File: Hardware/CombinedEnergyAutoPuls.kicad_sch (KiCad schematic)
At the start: 0 parts

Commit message: STAGE: Schematics finished
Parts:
- added A1: Arduino_Ethernet, Local_MCU_Module_Library:Arduino_Ethernet_WithMountingHoles, symbol Local_MCU_Module_Library:Arduino_Ethernet
- added C1: C10uf, Capacitor_SMD:C_0603_1608Metric, symbol Local_Device_Library:C10uf
- added C2: C330nf, Capacitor_SMD:C_0805_2012Metric, symbol Local_Device_Library:C330nf
- added C3: C100nf, Capacitor_SMD:C_0402_1005Metric, symbol Local_Device_Library:C100nf
- added D1, D2, D3, D4, D5, D6, D7, D8: 1N4148WS, Diode_SMD:D_SOD-323F, symbol Local_Diode_Library:1N4148WS
- added D10: D_Z2V7, Diode_THT:D_DO-34_SOD68_P7.62mm_Horizontal, symbol Local_Diode_Library:D_Z2V4
- added D11: 1N4004, Diode_THT:D_DO-41_SOD81_P12.70mm_Horizontal, symbol Local_Diode_Library:1N4004
- added D9: LED_G3, LED_THT:LED_D3.0mm, symbol Local_Diode_Library:LED_G3
- added J1, J2, J6: Screw_Terminal_01x04, Local_Connectors:TerminalBlock_PT-1,5-4-5.0-H_1x04_P5.00mm_Horizontal-(F.Mount), symbol Local_Connectors_Library:Screw_Terminal_01x04
- added J3: Arduino_USB-Serial_Card, Local_Connectors:Arduino_USB-Serial_Card, symbol Local_Connectors_Library:Arduino_USB-Serial_Card_Connector
- added J4: Arduino_USB-Serial_Card_Connector, Local_Connectors:Arduino_USB-Serial_Card_EdgeConn, symbol Local_Connectors_Library:Arduino_USB-Serial_Card_Connector
- added J5: AudioJack3_Switch, Local_Connectors:AUDIO_JACK_ASJ-195-L-HT-(F.Mount), symbol Local_Connectors_Library:AudioJack3_Switch
- added JP1: Jumper_3_Bridged12, Connector_PinHeader_2.54mm:PinHeader_1x03_P2.54mm_Vertical, symbol Local_Connectors_Library:Jumper_3_Bridged12
- added Q1: S8550_PNP, Package_TO_SOT_SMD:SOT-23, symbol Local_Transistor_BJT_Library:S8550_PNP
- added Q2, Q3: S8050_NPN, Package_TO_SOT_SMD:SOT-23, symbol Local_Transistor_BJT_Library:S8050_NPN
- added R1, R8, R9: R10K, Resistor_SMD:R_0402_1005Metric, symbol Local_Device_Library:R10K
- added R2: R680K, Resistor_SMD:R_0603_1608Metric, symbol Local_Device_Library:R680K
- added R3: R39K, Resistor_SMD:R_0402_1005Metric, symbol Local_Device_Library:R39K
- added R4, R5: R180K, Resistor_SMD:R_0603_1608Metric, symbol Local_Device_Library:R180K
- added R6: R220, Resistor_SMD:R_0805_2012Metric, symbol Local_Device_Library:R220
- added R7: R56, Resistor_SMD:R_1206_3216Metric, symbol Local_Device_Library:R56
- added U1: L78S05CV, Package_TO_SOT_THT:TO-220-3_Vertical, symbol Local_Miscellaneous_Library:L78S05CV
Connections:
- new net: Q1.1 (B), R2.2
- new net: Q1.3 (C), R4.1
- new net: D11.2 (A), J6.1 (Pin_1)
- new net: J5.1 (S), R8.2, R9.1
- new net: Q2.1 (B), R3.1, R4.2
- new net: A1.7 (A0), D3.1 (K), J2.2 (Pin_2)
- new net: D1.2 (A), D2.2 (A), D3.2 (A), D4.2 (A), D5.2 (A), D6.2 (A), D7.2 (A), D8.2 (A), R1.2, R2.1
- new net: A1.8 (A1), D2.1 (K), J2.3 (Pin_3)
- new net: A1.30 (N/C), J4.2 (N/C)
- new net: A1.32 (TXD), J4.4 (TXD)
- new net: A1.33 (RXD), J4.5 (RXD)
- new net: A1.34 (~{RTS}), J4.6 (DRT)
- new net: A1.19 (D6), D6.1 (K), J1.3 (Pin_3)
- new net: C1.1, J5.2 (T), JP1.3 (B), R7.1
- new net: A1.16 (D3/INT1), D8.1 (K), J1.1 (Pin_1)
- new net: A1.18 (D5), D7.1 (K), J1.2 (Pin_2)
- new net: A1.20 (D7), D5.1 (K), J1.4 (Pin_4)
- new net: A1.6 (VIN), C2.1, R6.1, U1.3 (VO)
- new net: D9.2 (A), R6.2
- new net: A1.21 (D8), D4.1 (K), J2.1 (Pin_1)
- new net: D1.1 (K), J2.4 (Pin_4), JP1.1 (A)
- new net: D9.1 (K), Q3.3 (C)
- new net: A1.15 (D2/INT0), Q2.3 (C)
- new net: A1.10 (A3), R5.1
- new net: Q3.1 (B), R5.2
- new net: A1.9 (A2), JP1.2 (C)
- new net +24V: C3.1, D11.1 (K), U1.1 (VI)
- new net +5V: A1.3 (+5V), Q1.2 (E), R1.1, R8.1
- new net GND: A1.27 (GND), A1.29 (GND_BLK), A1.4 (GND), A1.5 (GND), C1.2, D10.2 (A), J4.1 (GND), J5.5 (R), J6.2 (Pin_2), Q2.2 (E), Q3.2 (E), R3.2, R7.2, R9.2
- new net GND1: C2.2, C3.2, D10.1 (K), U1.2 (GND)
- new net VCC: A1.31 (VCC), J4.3 (VCC)
- no-connect marks 0 -> 25

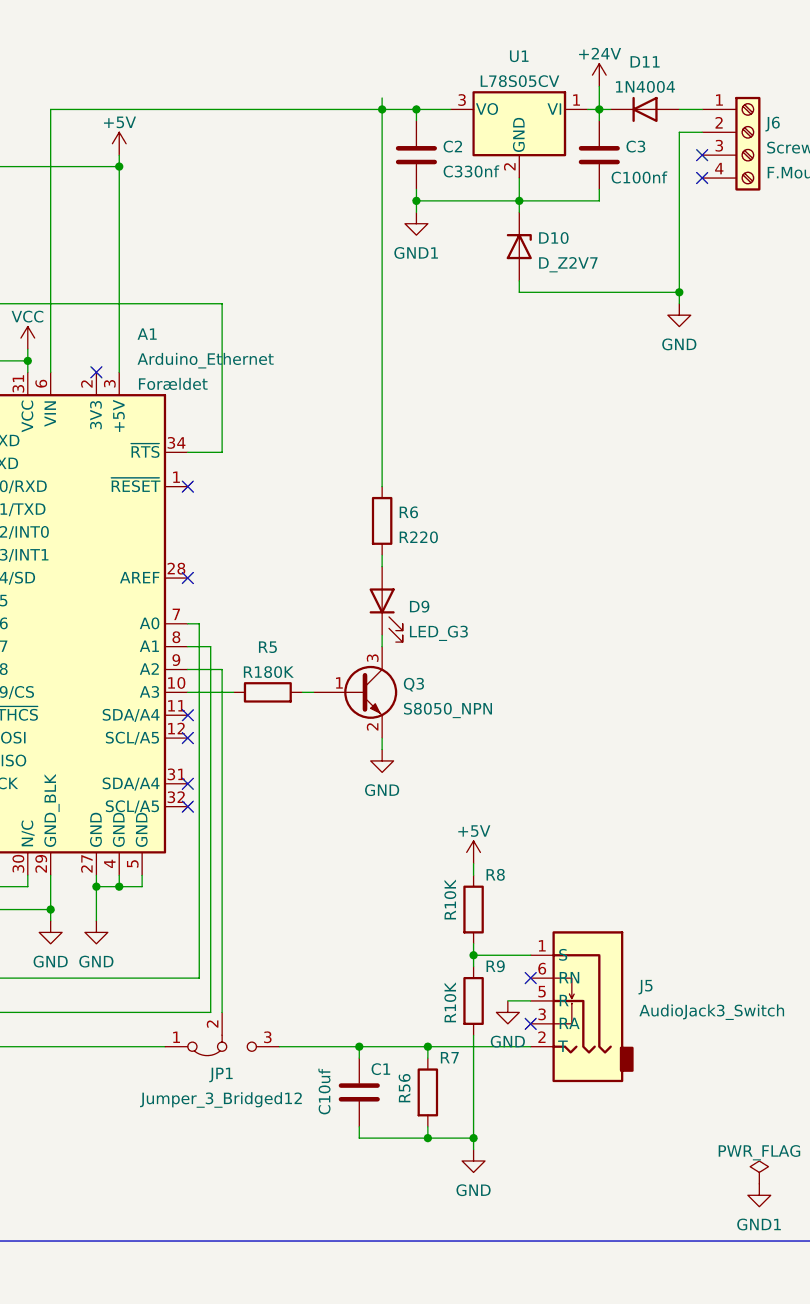
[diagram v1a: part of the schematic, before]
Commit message: FIX: Fixes made to local libraies
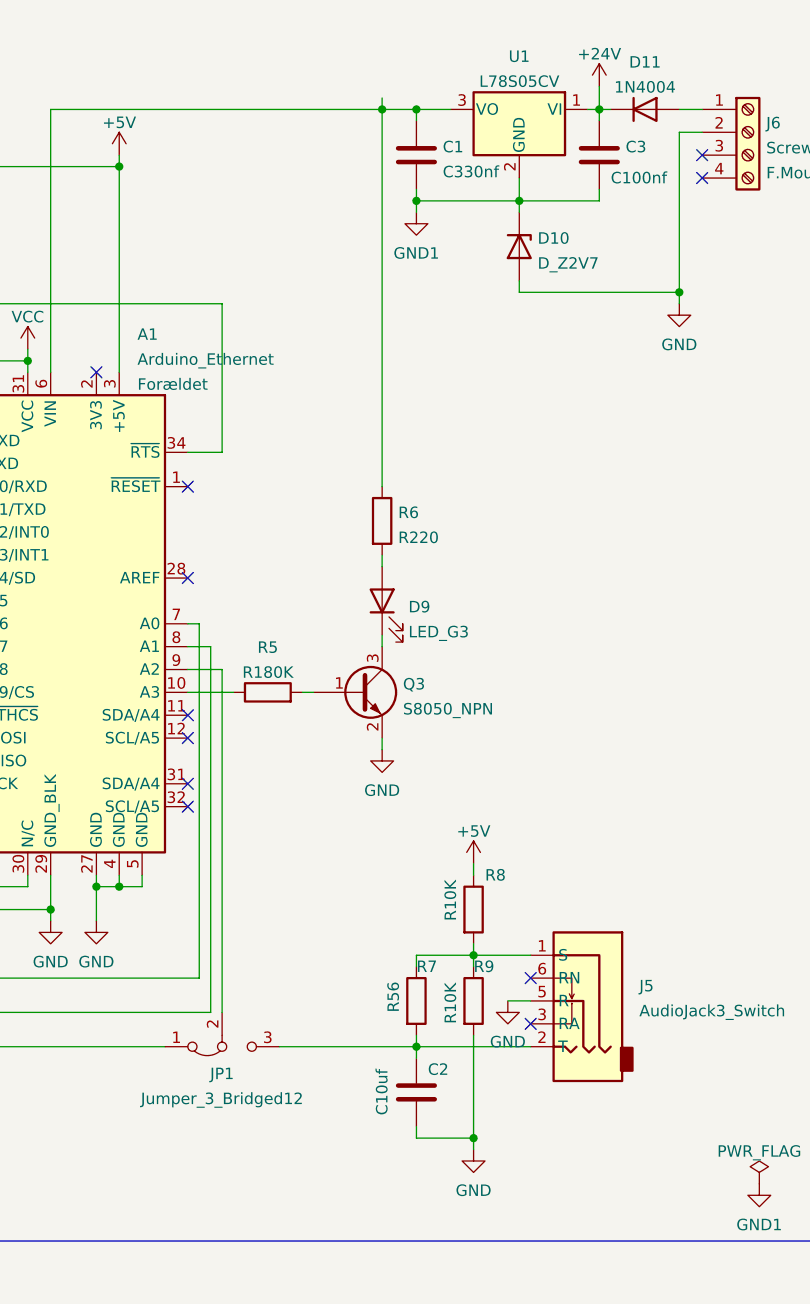
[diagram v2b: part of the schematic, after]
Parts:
- renumbered C2 to C1, C1 to C2
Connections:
- net GND: no longer R7.2
- net at J5.1 (S), R8.2, R9.1: now also R7.1
- net at C2.1, J5.2 (T), JP1.3 (B): now also R7.2; no longer R7.1
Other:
- moved on the sheet: C2, R7

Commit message: Schematics and components placed on BCB for autoStart added to the project.
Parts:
- added C101: C10nf, Capacitor_SMD:C_0402_1005Metric, symbol Local_Device_Library:C10nf
- added C102, C103, C104: C100nf, Capacitor_SMD:C_0402_1005Metric, symbol Local_Device_Library:C100nf
- added C105: C330nf, Capacitor_SMD:C_0805_2012Metric, symbol Local_Device_Library:C330nf
- added D101: 1N4148WS, Diode_SMD:D_SOD-323F, symbol Local_Diode_Library:1N4148WS
- added J101: AudioJack3_Switch, Local_Connectors:AUDIO_JACK_ASJ-195-L-HT-(B.Mount), symbol Local_Connectors_Library:AudioJack3_Switch
- added J102: Screw_Terminal_01x03, Local_Connectors:Phoenix_TERM_BLOCK_3POS_45DEG_5MM_PCB-(B.Mount), symbol Local_Connectors_Library:Screw_Terminal_01x03
- added J103: Conn_3P, Local_Connectors:PinHeader_1x03_P_5mm_Vertical-(F.Mount), symbol Local_Connectors_Library:Conn_3P
- added J3: Pin_Header_1x6, Local_Connectors:PinHeader_1x06_P_0,1in_Vertical, symbol Local_Connectors_Library:Pin_Header_1x6
- added Q101: S8050, Package_TO_SOT_SMD:SOT-23, symbol Local_Transistor_BJT_Library:S8050_NPN
- added R101, R102, R103: R10K, Resistor_SMD:R_0402_1005Metric, symbol Local_Device_Library:R10K
- added R104: R330K, Resistor_SMD:R_0402_1005Metric, symbol Local_Device_Library:R330K
- added R105: R100K, Resistor_SMD:R_0402_1005Metric, symbol Local_Device_Library:R100K
- added R106: R680K, Resistor_SMD:R_0603_1608Metric, symbol Local_Device_Library:R680K
- added R107: R150K, Resistor_SMD:R_0402_1005Metric, symbol Local_Device_Library:R150K
- added R108: R33K, Resistor_SMD:R_0402_1005Metric, symbol Local_Device_Library:R33K
- added R109: R180K, Resistor_SMD:R_0603_1608Metric, symbol Local_Device_Library:R180K
- added U101: LM358DR2G, Package_SO:SOIC-8_3.9x4.9mm_P1.27mm, symbol Local_Miscellaneous_Library:LM358DR2G
- added U102: 78L05, Package_TO_SOT_SMD:SOT-89-3, symbol Local_Miscellaneous_Library:78L05
- renumbered J3 to J4, J4 to J5, J5 to J6, J6 to J7
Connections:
- net GND3: now reaches J4.1 (GND)
- net GND3: now also J3.1 (Pin_1)
- net at J4.2 (N/C): now also J3.2 (Pin_2)
- net VCC1: now reaches J4.3 (VCC)
- net VCC1: now also J3.3 (Pin_3)
- net at J4.4 (TXD): now also J3.4 (Pin_4)
- net at J4.5 (RXD): now also J3.5 (Pin_5)
- net at J4.6 (DRT): now also J3.6 (Pin_6)
- new net: C103.2, D101.1 (K), R106.1, U101.5 (+)
- new net: R107.2, R108.1, U101.6 (-)
- new net: R109.1, U101.7
- new net: J102.2 (Pin_2), J103.2 (Pin_2), Q101.3 (C)
- new net: C102.2, D101.2 (A), R105.1
- new net: J101.1 (S), R101.1
- new net: C101.1, R101.2, R104.1, U101.3 (+)
- new net: C101.2, C102.1, R104.2, U101.1
- new net: J101.2 (T), R102.2, R103.1, U101.2 (-)
- new net: Q101.1 (B), R109.2
- new net GND2: C103.1, C104.1, C105.2, J101.5 (R), J102.1 (Pin_1), J103.1 (Pin_1), Q101.2 (E), R103.2, R105.2, R106.2, R108.2, U101.4 (V-), U102.2 (GND)
- new net VS: C104.2, R102.1, R107.1, U101.8 (V+), U102.1 (OUT)
- new net VSS: C105.1, J102.3 (Pin_3), J103.3 (Pin_3), U102.3 (IN)
- no-connect marks 25 -> 21
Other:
- moved on the sheet: J4

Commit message: UPD: - Schematics and components placed on BCB for ProgrameablePulseGenerator added to the project
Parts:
- removed J4: Arduino_USB-Serial_Card, Local_Connectors:Arduino_USB-Serial_Card, symbol Local_Connectors_Library:Arduino_USB-Serial_Card_Connector
- removed J5: Arduino_USB-Serial_Card_Connector, Local_Connectors:Arduino_USB-Serial_Card_EdgeConn, symbol Local_Connectors_Library:Arduino_USB-Serial_Card_Connector
- added A201: Arduino_Nano_v3, Module:Arduino_Nano, symbol Local_MCU_Module_Library:Arduino_Nano_v3
- added AE201: Antenna, Local_Misckllaneous_Library:Undefined_Antenna(B.Mount), symbol Local_Miscellaneous_Library:Antenna
- added C201: C100nf, Capacitor_SMD:C_0402_1005Metric, symbol Local_Device_Library:C100nf
- added C202: C330nf, Capacitor_SMD:C_0805_2012Metric, symbol Local_Device_Library:C330nf
- added D201, D203, D205, D207, D209, D211, D213, D215, D217, D219: 1N4148WS, Diode_SMD:D_SOD-323F, symbol Local_Diode_Library:1N4148WS
- added D202, D204, D206, D208, D210, D212, D214, D216, D218, D220: LED, LED_SMD:LED_0805_2012Metric, symbol Local_Diode_Library:LED_0805_R
- added J201, J202: Conn_20P_Female, Connector_PinHeader_2.54mm:PinHeader_1x20_P2.54mm_Vertical, symbol Local_Connectors_Library:Conn_20P_Female
- added J203, J204: Conn_4P_Female, Connector_PinHeader_2.54mm:PinHeader_1x04_P2.54mm_Vertical, symbol Local_Connectors_Library:Conn_4P_Female
- added J205: Barrel_Jack_Switch, Local_Connectors:BarrelJack_Horizontal(F.Mount), symbol Local_Connectors_Library:Barrel_Jack_Switch
- added J4: Arduino_USB-Serial_Card_Connector, Local_Connectors:Arduino_USB-Serial_Card, symbol Local_Connectors_Library:Arduino_USB-Serial_Card-Edge_Connector
- added J5: Arduino_USB-Serial_Edge_Connector, Local_Connectors:Arduino_USB-Serial_Card_EdgeConn, symbol Local_Connectors_Library:Arduino_USB-Serial_Card-Edge_Connector
- added JP201, JP202, JP203, JP204, JP205, JP206, JP207, JP208, JP209, JP210: SolderJumper, Local_Connectors:SolderJumper-2_P1.3mm_Bridged_RoundedPad1.0x1.5mm(B.Mount), symbol Local_Connectors_Library:SolderJumper_2_Bridged
- added JP211: Jumper_3_Bridged12, Connector_PinHeader_2.54mm:PinHeader_1x03_P2.54mm_Vertical, symbol Local_Connectors_Library:Jumper_3_Bridged12
- added R201, R203, R205, R207, R209, R211, R213, R215, R217, R219, R221: R390, Resistor_SMD:R_0603_1608Metric, symbol Local_Device_Library:R390
- added R202, R204, R206, R208, R210, R212, R214, R216, R218, R220: R180, Resistor_SMD:R_0805_2012Metric, symbol Local_Device_Library:R180
- added SW201: THT_SW_4_Tactile, Local_Misckllaneous_Library:THT_SW_Tactile(F.Mount), symbol Local_Miscellaneous_Library:THT_SW_4_Tactile
- added U201, U202, U203, U204, U205, U206, U207, U208, U209, U210, U211: PC817, Local_Misckllaneous_Library:DIP-4_W7.62mm_Slim(F.Mount), symbol Local_Miscellaneous_Library:PC817
- added U212: L78S05CV, Package_TO_SOT_THT:TO-220-3_Vertical, symbol Local_Miscellaneous_Library:L78S05CV
- D10: value D_Z2V7 -> D_Z2V4; footprint Diode_THT:D_DO-34_SOD68_P7.62mm_Horizontal -> Diode_THT:D_DO-35_SOD27_P7.62mm_Horizontal; JLCPCB Part # C294824 -> C2504; MFR. Part # GDZJ12C_AY_10001 -> BZX55C2V4; Manufacturer PANJIT International -> ST(Semtech)
- J101, J102, J103, J3: now left out of the parts list
- Q101: value S8050 -> S8050_NPN
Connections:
- net GND: now also J5.1 (GND)
- net GND3: now also J4.1 (GND)
- net VCC: now also J5.3 (VCC)
- net VCC1: now also J4.3 (VCC)
- net at A1.30 (N/C): now also J5.2 (N/C)
- net at A1.33 (RXD): now also J5.5 (RXD)
- net at A1.34 (~{RTS}): now also J5.6 (DRT)
- net at J3.2 (Pin_2): now also J4.2 (N/C)
- net at J3.4 (Pin_4): now also J4.4 (TXD)
- net at J3.5 (Pin_5): now also J4.5 (RXD)
- net at J3.6 (Pin_6): now also J4.6 (DRT)
- new net: R203.2, U202.1
- new net: JP211.2 (C), R202.1, R204.1, R206.1, R208.1, R210.1, R212.1, R214.1, R216.1, R218.1, R220.1
- new net: C201.1, JP211.3 (B), U212.3 (VO)
- new net: D204.2 (A), R204.2
- new net: A201.14 (D11), D220.1 (K), J201.19 (Pin_19), J201.20 (Pin_20), U210.2
- new net: D220.2 (A), R220.2
- new net: R201.2, U201.1
- new net: A201.5 (D2), D202.1 (K), J201.1 (Pin_1), J201.2 (Pin_2), U201.2
- new net: J202.1 (Pin_1), J202.2 (Pin_2), JP201.2 (B), U201.4
- new net: D209.1 (K), JP205.1 (A)
- new net: D201.2 (A), D203.2 (A), D205.2 (A), D207.2 (A), D209.2 (A), D211.2 (A), D213.2 (A), D215.2 (A), D217.2 (A), D219.2 (A), U211.2
- new net: R217.2, U209.1
- new net: A201.6 (D3), D204.1 (K), J201.3 (Pin_3), J201.4 (Pin_4), U202.2
- new net: A201.8 (D5), D208.1 (K), J201.7 (Pin_7), J201.8 (Pin_8), U204.2
- new net: D208.2 (A), R208.2
- new net: R221.2, U211.1
- new net: A201.13 (D10), D218.1 (K), J201.17 (Pin_17), J201.18 (Pin_18), U209.2
- new net: J202.17 (Pin_17), J202.18 (Pin_18), JP209.2 (B), U209.4
- new net: D202.2 (A), R202.2
- new net: D218.2 (A), R218.2
- new net: D214.2 (A), R214.2
- new net: A201.24 (A5), SW201.1, SW201.2
- new net: D215.1 (K), JP208.1 (A)
- new net: R219.2, U210.1
- new net: R213.2, U207.1
- new net: D207.1 (K), JP204.1 (A)
- new net: J202.7 (Pin_7), J202.8 (Pin_8), JP204.2 (B), U204.4
- new net: D205.1 (K), JP203.1 (A)
- new net: D213.1 (K), JP207.1 (A)
- new net: J202.13 (Pin_13), J202.14 (Pin_14), JP207.2 (B), U207.4
- new net: D211.1 (K), JP206.1 (A)
- new net: J202.11 (Pin_11), J202.12 (Pin_12), JP206.2 (B), U206.4
- new net: D217.1 (K), JP209.1 (A)
- new net: R209.2, U205.1
- new net: A201.9 (D6), D210.1 (K), J201.10 (Pin_10), J201.9 (Pin_9), U205.2
- new net: J202.10 (Pin_10), J202.9 (Pin_9), JP205.2 (B), U205.4
- new net: A201.7 (D4), D206.1 (K), J201.5 (Pin_5), J201.6 (Pin_6), U203.2
- new net: D206.2 (A), R206.2
- new net: J202.19 (Pin_19), J202.20 (Pin_20), JP210.2 (B), U210.4
- new net: R205.2, U203.1
- new net: J202.5 (Pin_5), J202.6 (Pin_6), JP203.2 (B), U203.4
- new net: R215.2, U208.1
- new net: J203.3 (Pin_3), J204.3 (Pin_3)
- new net: J203.4 (Pin_4), J204.4 (Pin_4), U211.4
- new net: D203.1 (K), JP202.1 (A)
- new net: J202.3 (Pin_3), J202.4 (Pin_4), JP202.2 (B), U202.4
- new net: J202.15 (Pin_15), J202.16 (Pin_16), JP208.2 (B), U208.4
- new net: D216.2 (A), R216.2
- new net: D219.1 (K), JP210.1 (A)
- new net: R211.2, U206.1
- new net: A201.12 (D9), D216.1 (K), J201.15 (Pin_15), J201.16 (Pin_16), U208.2
- new net: R207.2, U204.1
- new net: A1.32 (TXD), J5.4 (TXD)
- new net: A201.19 (A0), AE201.1 (A)
- new net: D212.2 (A), R212.2
- new net: D210.2 (A), R210.2
- new net: A201.11 (D8), D214.1 (K), J201.13 (Pin_13), J201.14 (Pin_14), U207.2
- new net: A201.10 (D7), D212.1 (K), J201.11 (Pin_11), J201.12 (Pin_12), U206.2
- new net: D201.1 (K), JP201.1 (A)
- new net Arduino_5V: A201.27 (+5V), JP211.1 (A), R201.1, R203.1, R205.1, R207.1, R209.1, R211.1, R213.1, R215.1, R217.1, R219.1, R221.1
- new net GND4: A201.29 (GND), A201.4 (GND), C201.2, C202.2, J203.1 (Pin_1), J204.1 (Pin_1), J205.2, SW201.3 (K), SW201.4 (A), U201.3, U202.3, U203.3, U204.3, U205.3, U206.3, U207.3, U208.3, U209.3, U210.3, U211.3, U212.2 (GND)
- new net Vin: A201.30 (VIN), C202.1, J203.2 (Pin_2), J204.2 (Pin_2), J205.1, U212.1 (VI)
- no-connect marks 21 -> 36

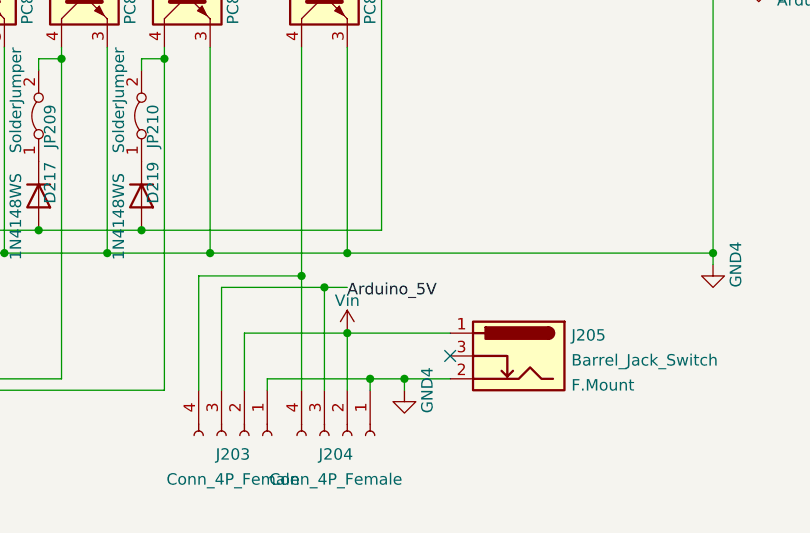
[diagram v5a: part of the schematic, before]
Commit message: UPD: Silkmask references modified
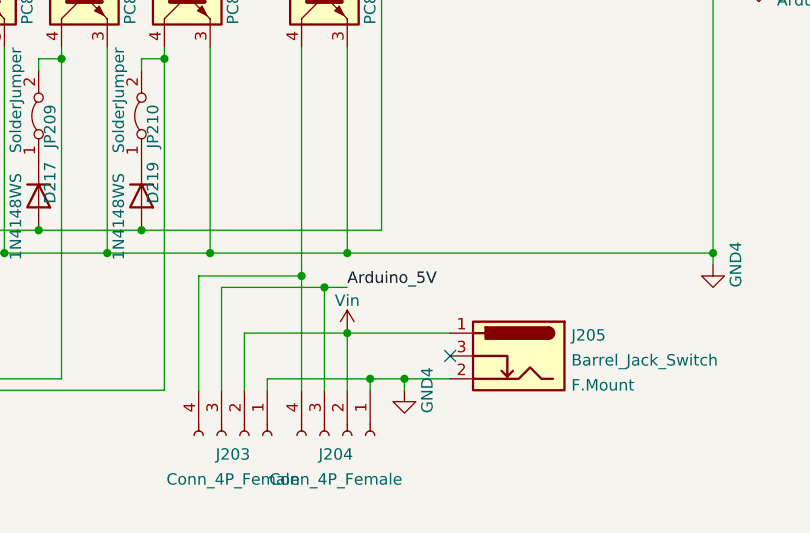
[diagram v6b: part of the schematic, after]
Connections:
- net Arduino_5V: now also J203.3 (Pin_3), J204.3 (Pin_3)
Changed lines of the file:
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@@
     (effects (font (size 1.27 1.27)) (justify left bottom))
   )
-  (label "Arduino_5V" (at 172.72 259.08 0)
+  (label "Arduino_5V" (at 172.72 257.81 0)
     (effects (font (size 1.27 1.27)) (justify left bottom))
   )
